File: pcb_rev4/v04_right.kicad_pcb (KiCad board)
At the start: 2 copper layers, 170.7 x 131.2 mm, 74 parts, among them J1 Audio-Jack-4, SW1 SW_Push, U1 ProMicro

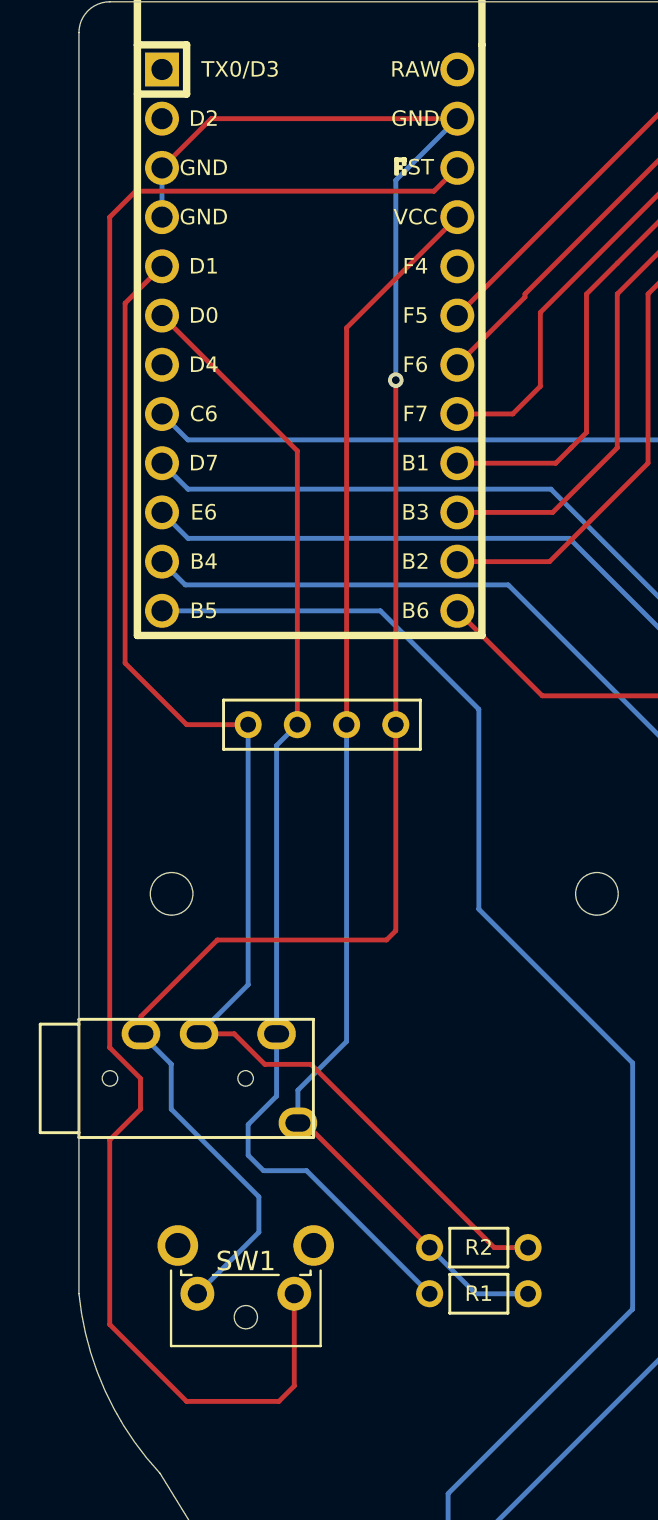
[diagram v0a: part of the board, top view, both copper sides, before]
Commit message: Fixed footprint for TRRS jack in right side and rerouted.
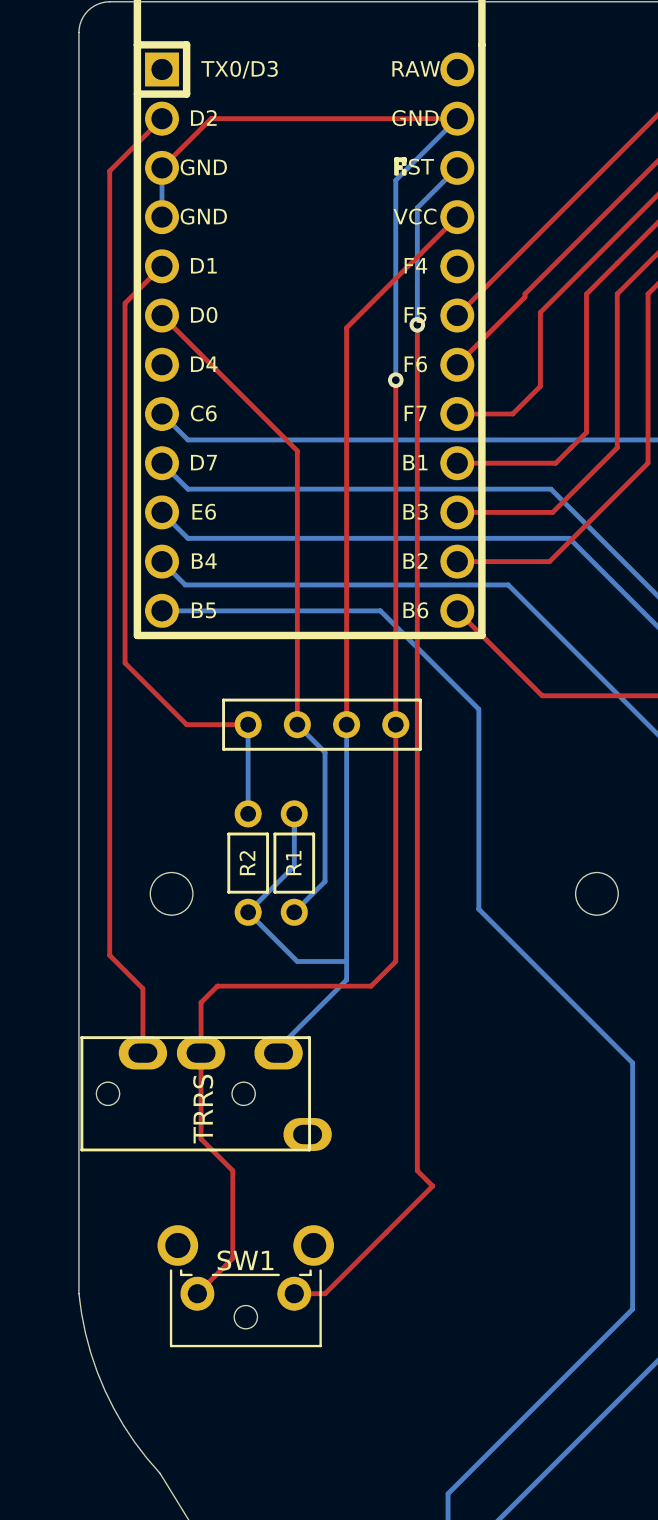
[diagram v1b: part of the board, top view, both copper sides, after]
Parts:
- removed J1: Audio-Jack-4, Keebio-Parts:TRRS-PJ-320A
- added TRRS1: MJ-4PP-9, kbd:MJ-4PP-9_1side, F.Cu at (-186.5, 80.2)
- moved R1 24.2 mm to (-175.4, 68.3), turned to 90 degrees
- moved R2 23.1 mm to (-177.8, 68.3), turned to 270 degrees
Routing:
- net DATA: track 0.00 -> 50.1 mm
- net SDA: track 67.5 -> 33.5 mm
- net RESET: track 93.7 -> 63.2 mm, vias 0 -> 1
- net SCL: track 59.8 -> 35.2 mm
- net VCC: track 66.7 -> 60.2 mm
- net GND: track 95.2 -> 91.0 mm

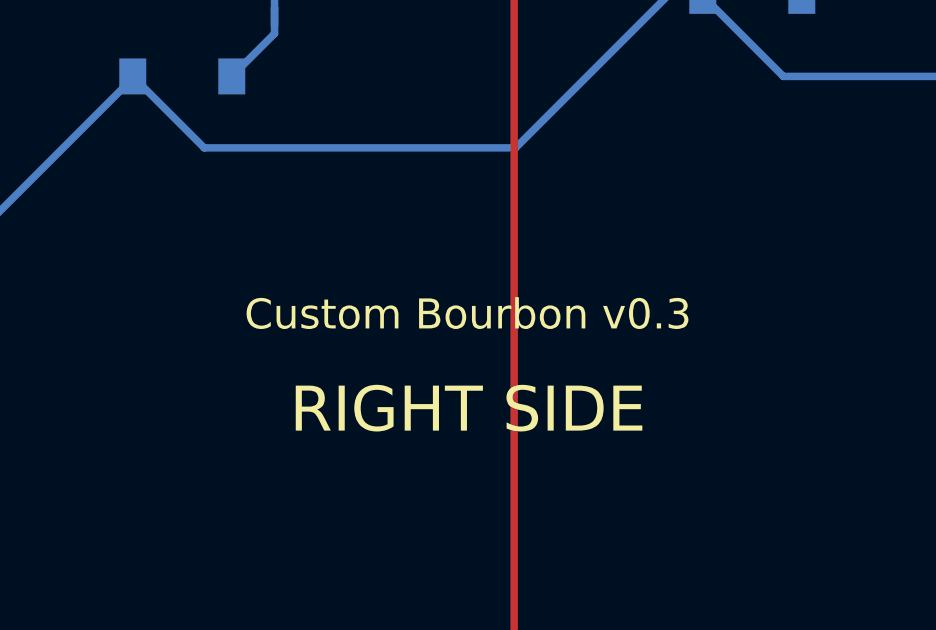
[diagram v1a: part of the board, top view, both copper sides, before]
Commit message: Updated silks for v0.4
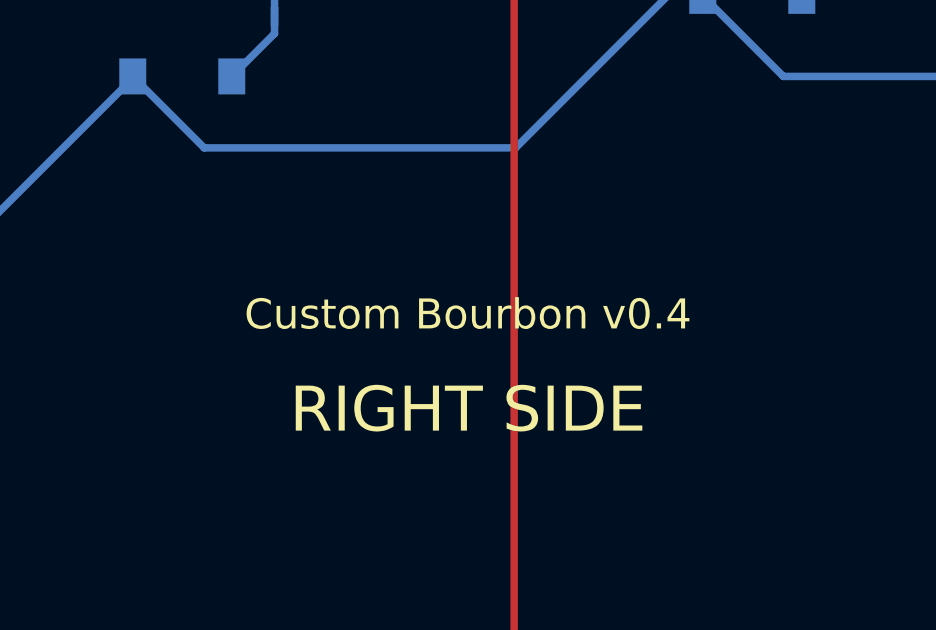
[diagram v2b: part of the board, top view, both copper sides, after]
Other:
- board text added: "Custom Bourbon v0.4"
- board text removed: "Custom Bourbon v0.3"

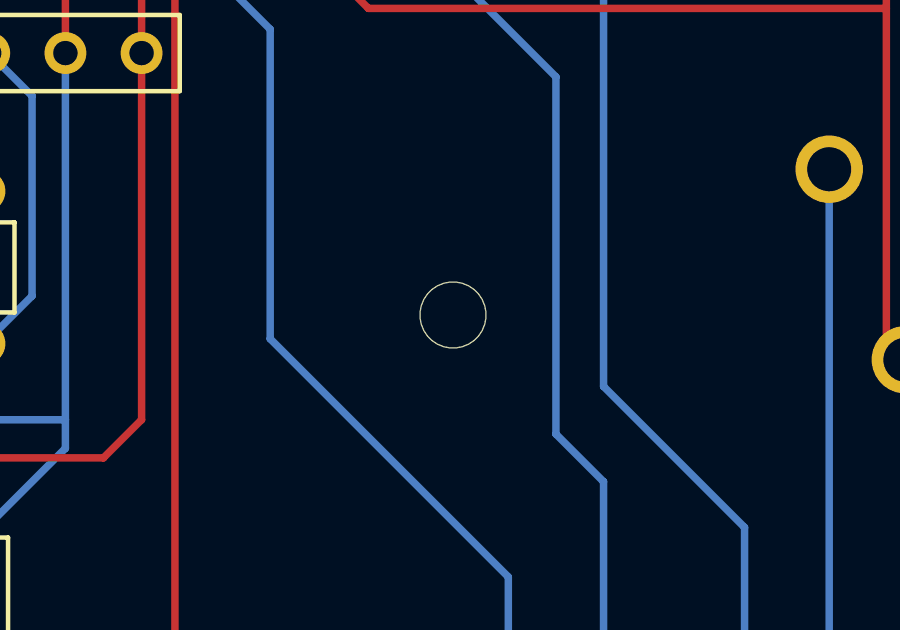
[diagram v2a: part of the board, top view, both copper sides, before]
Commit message: Moved the OLED cover holes slightly for better fit
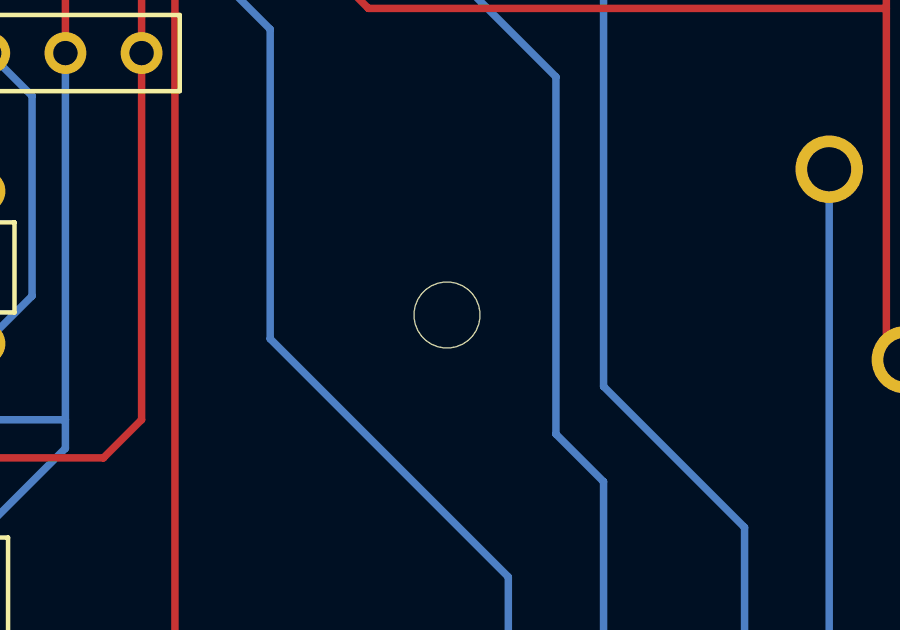
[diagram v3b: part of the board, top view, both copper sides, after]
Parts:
- moved H2 0.20 mm to (-160.0, 69.8)

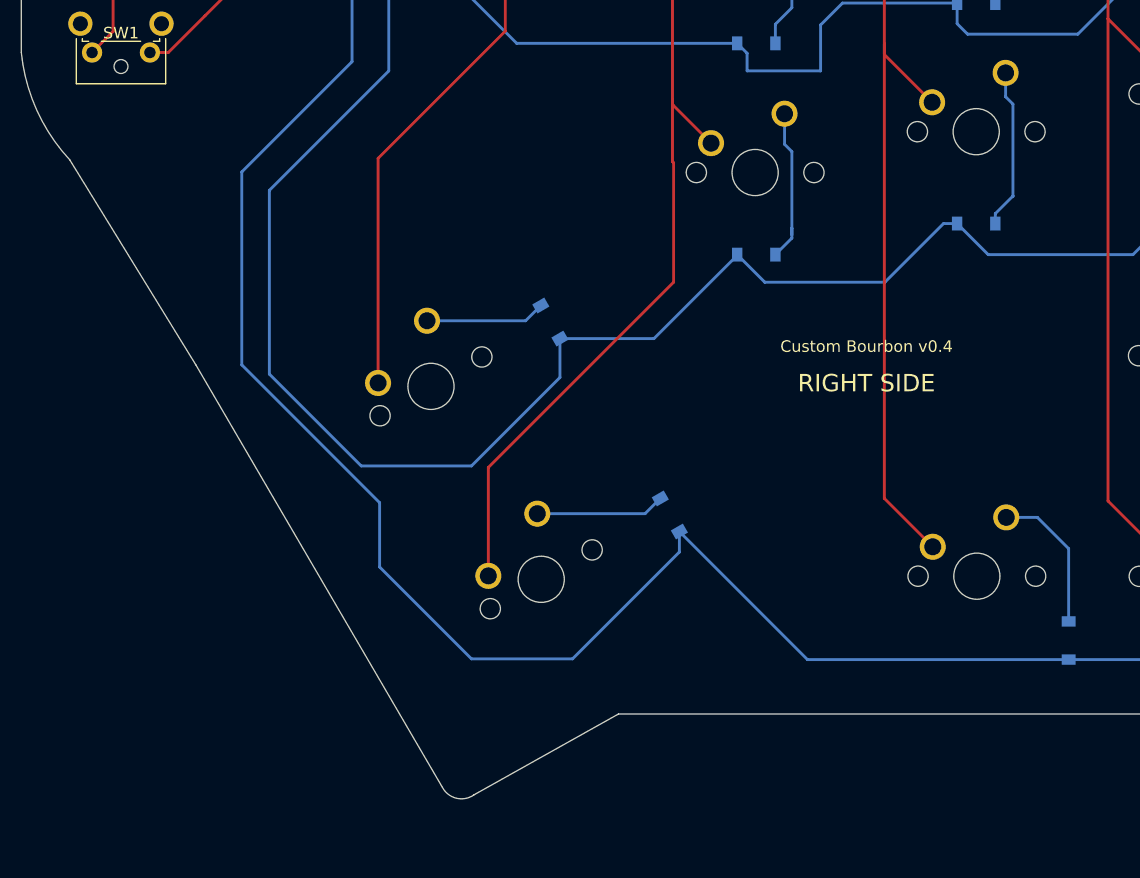
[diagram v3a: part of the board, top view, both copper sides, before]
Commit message: Repositioned both thumb clusters; fixed positioning of z key on left side
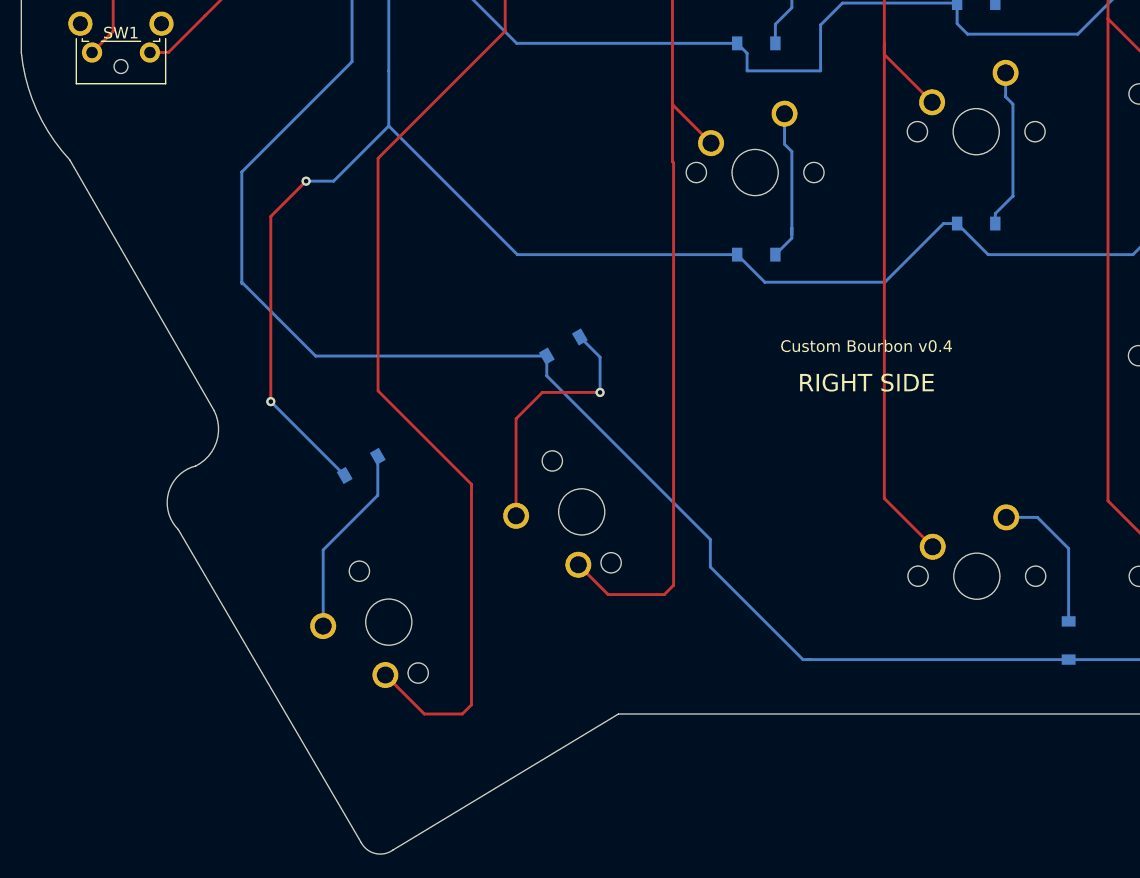
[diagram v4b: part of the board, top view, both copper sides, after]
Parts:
- moved MX36 20.7 mm to (-154.8, 139.7), turned to 120 degrees
- moved D36 20.5 mm to (-157.2, 126.2), turned to 30 degrees
- moved D45 17.2 mm to (-139.7, 115.9), turned to 30 degrees
- moved MX45 6.80 mm to (-138.1, 130.2), turned to 120 degrees
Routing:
- net col6: track 107.7 -> 148.1 mm
- net row4: track 262.6 -> 247.8 mm
- net Net-(D45-Pad2): track 11.2 -> 22.1 mm, vias 0 -> 1
- net Net-(D36-Pad2): track 10.4 -> 16.6 mm
- net row3: track 263.5 -> 257.7 mm, vias 0 -> 2
- net col5: track 181.3 -> 185.1 mm
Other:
- board size 170.7 x 131.2 mm -> 170.7 x 135.9 mm
